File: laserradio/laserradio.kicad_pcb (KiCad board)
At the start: 2 copper layers, 84 parts, among them J1 USB4105-GF-A, J2 Conn_01x01_Female, J3 DEBUG, J4 RIGHT, SW1 SW_SPDT, SW2 SW_SPDT, U1 W25Q128JV, U2 RP2040, U3 MCP1702T-3302E_CB, U4 ADA4891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

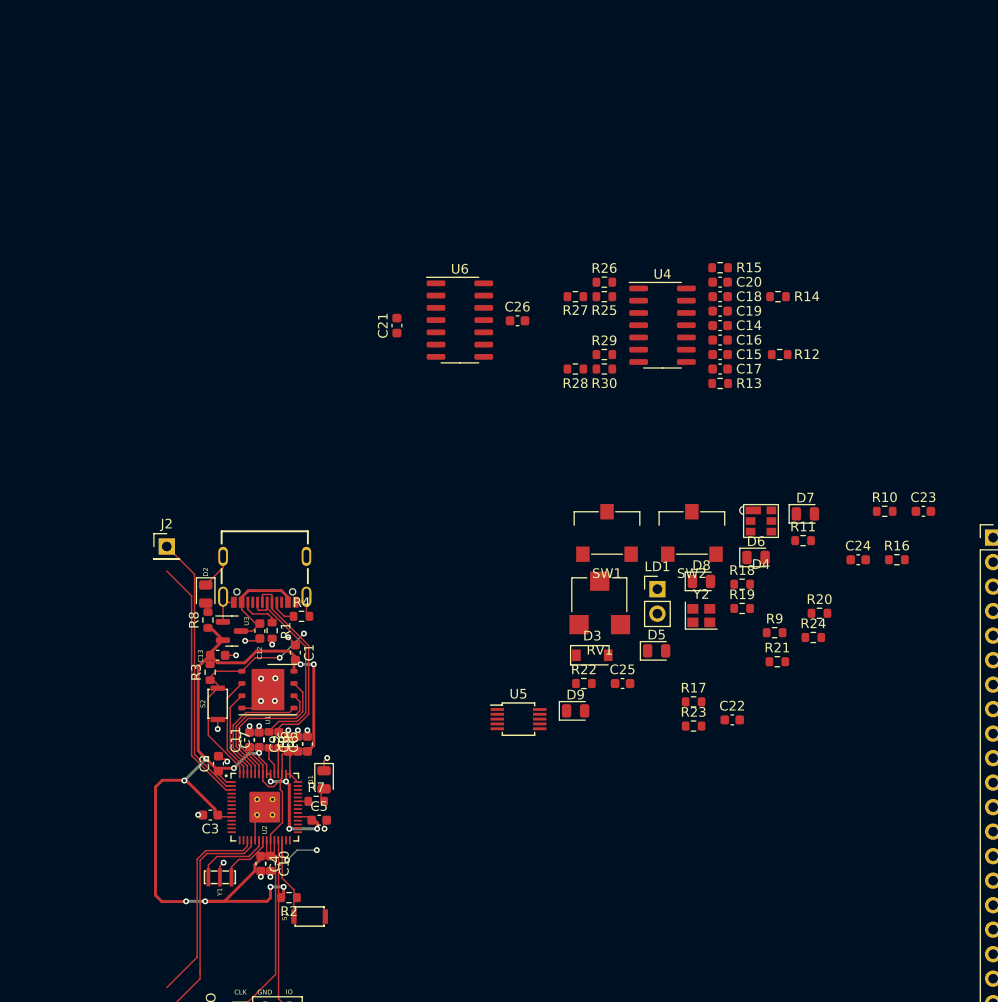
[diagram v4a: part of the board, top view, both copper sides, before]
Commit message: wip arranging op-amp filters
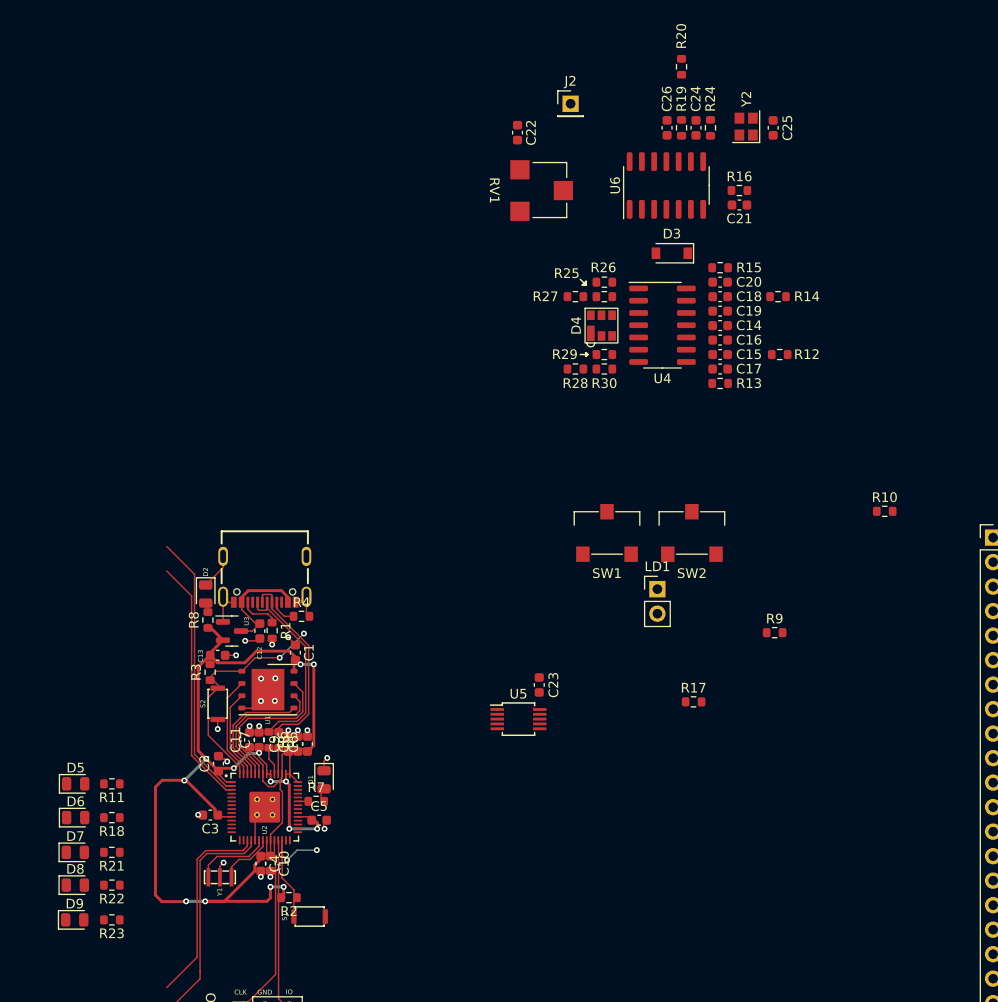
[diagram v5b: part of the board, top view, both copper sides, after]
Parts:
- moved D7 83.4 mm to (94.7, 104.6)
- moved R11 76.0 mm to (98.5, 97.5), turned to 180 degrees
- moved D6 75.5 mm to (94.7, 101.0)
- moved D8 72.1 mm to (94.7, 108.0)
- moved R21 71.8 mm to (98.5, 104.6), turned to 180 degrees
- moved R18 69.7 mm to (98.5, 101.0), turned to 180 degrees
- moved C22 64.8 mm to (140.5, 30.0), turned to -90 degrees
- moved R23 63.6 mm to (98.5, 111.6), turned to 180 degrees
- moved J2 62.1 mm to (146.0, 27.0)
- moved D5 61.8 mm to (94.7, 97.5)
- moved C25 59.7 mm to (167.0, 29.5), turned to 90 degrees
- moved R20 58.4 mm to (157.5, 23.2), turned to 90 degrees
- moved D9 56.3 mm to (94.6, 111.6)
- moved R24 53.9 mm to (160.5, 29.5), turned to -90 degrees
- moved R22 53.2 mm to (98.5, 108.0), turned to 180 degrees
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
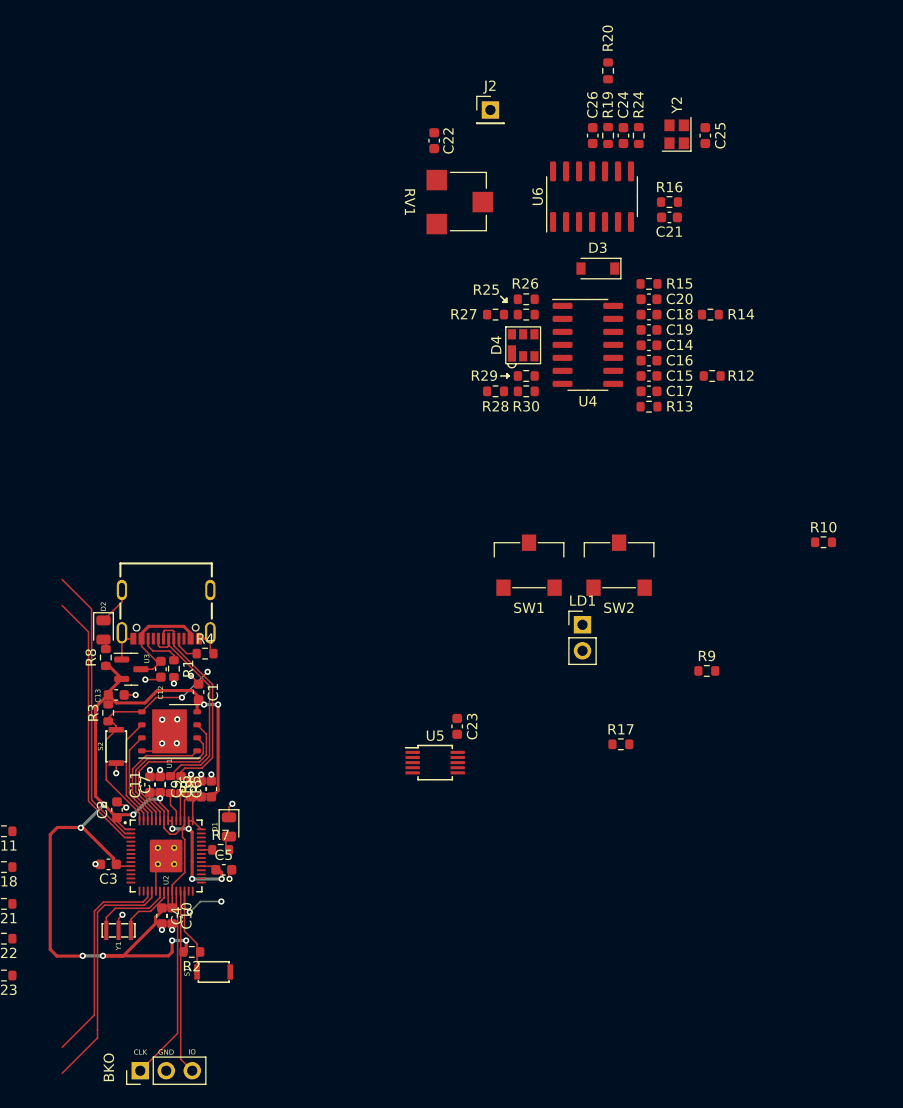
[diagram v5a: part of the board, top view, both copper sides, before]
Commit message: finish first pass of laying out components
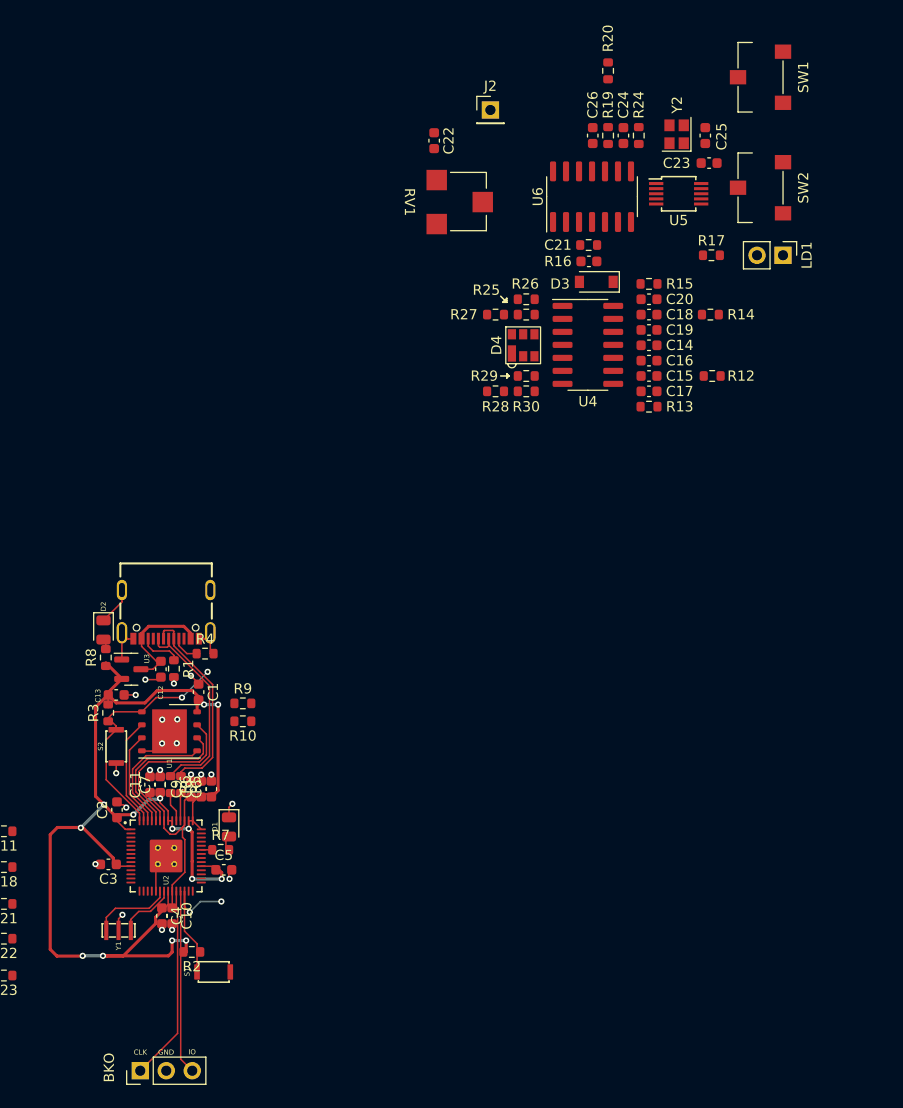
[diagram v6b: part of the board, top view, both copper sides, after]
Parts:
- moved U5 60.5 mm to (164.4, 35.2)
- moved C23 60.3 mm to (167.4, 32.2), turned to 0 degrees
- moved R10 59.4 mm to (121.8, 86.8), turned to 180 degrees
- moved SW1 52.8 mm to (172.4, 23.8), turned to 90 degrees
- moved R17 48.6 mm to (167.6, 41.2)
- moved R9 45.5 mm to (121.8, 85.0)
- moved LD1 41.1 mm to (174.6, 41.2), turned to -90 degrees
- moved SW2 39.4 mm to (172.4, 34.6), turned to 90 degrees
- moved C21 8.97 mm to (155.6, 41.8), turned to 0 degrees
- moved R16 8.95 mm to (155.6, 40.2), turned to 180 degrees
- moved D3 1.31 mm to (156.3, 43.8)
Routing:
- net +3V3: track 230.9 -> 203.0 mm
- net /Tx: track 25.8 -> 0.00 mm
- net /GPIO15: track 23.7 -> 0.00 mm
- net /GPIO14: track 21.0 -> 0.00 mm

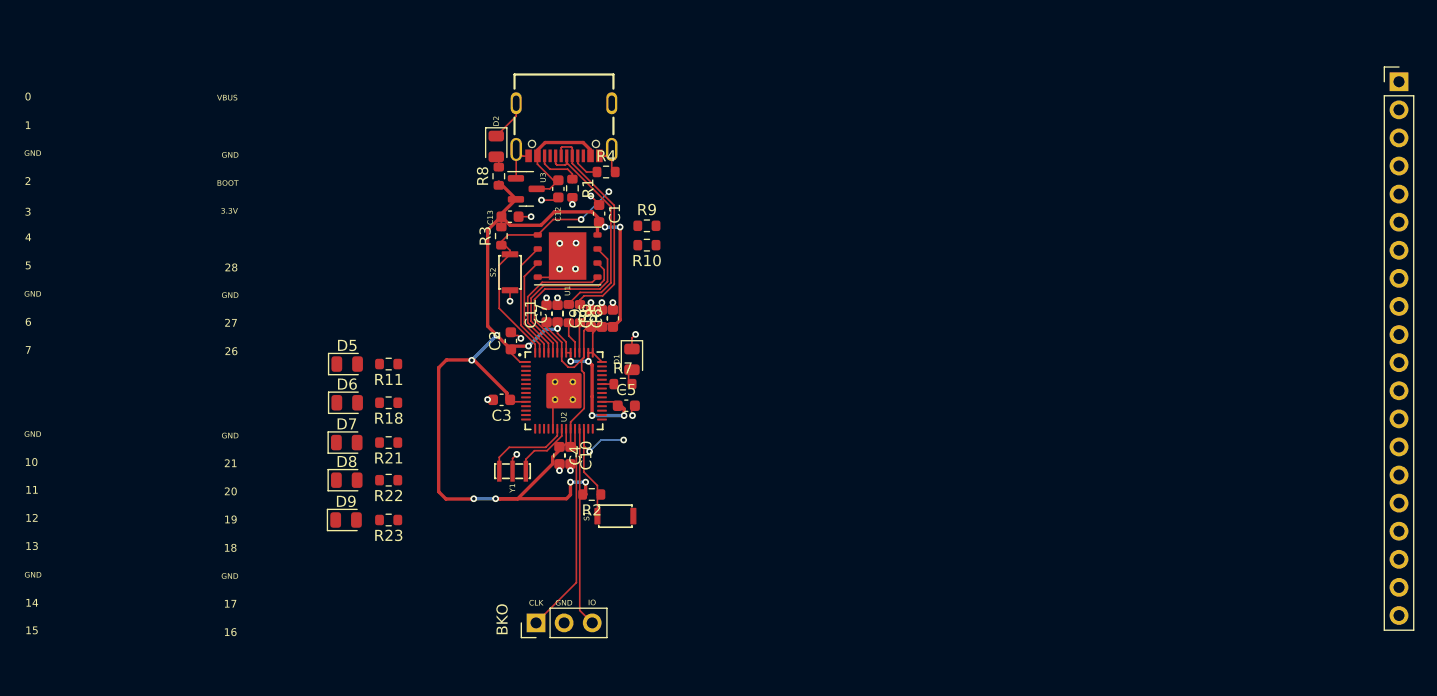
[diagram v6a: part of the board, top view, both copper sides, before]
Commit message: Refactored MP3 circuit
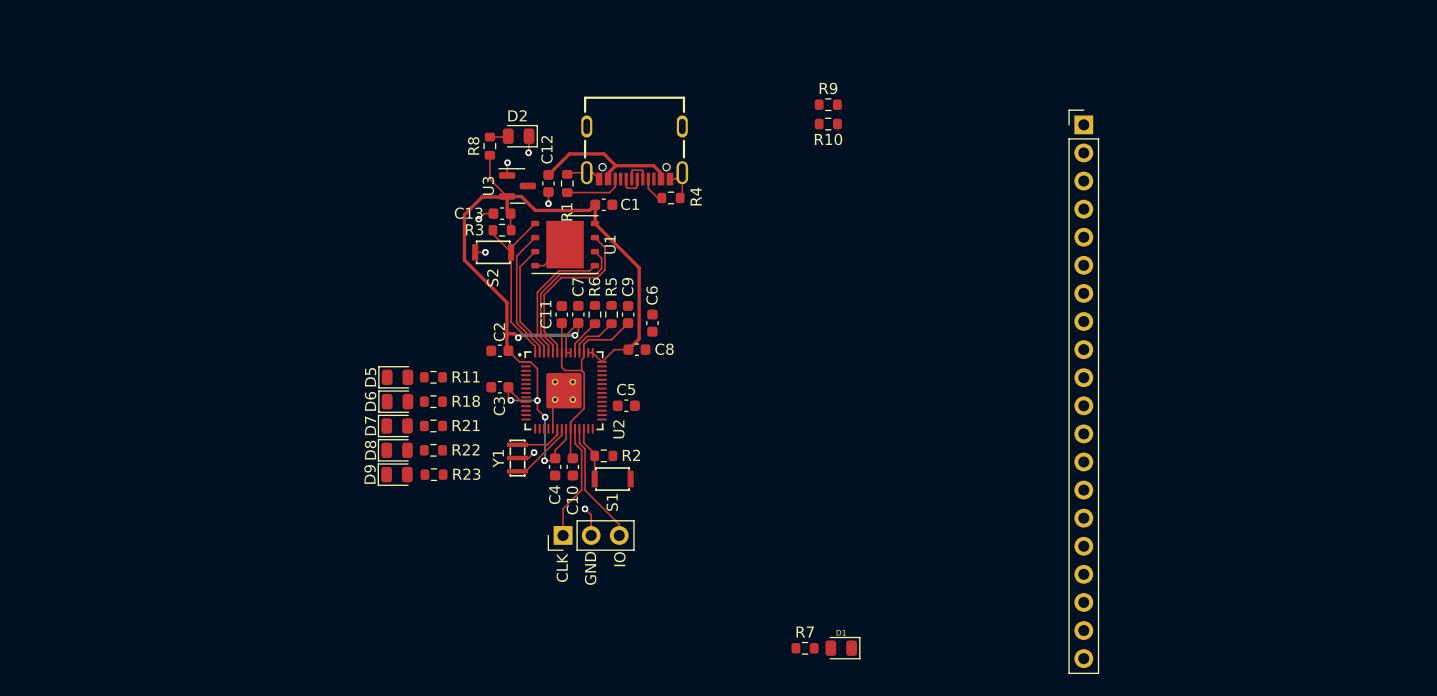
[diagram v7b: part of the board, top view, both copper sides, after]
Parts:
- moved D1 32.2 mm to (139.4, 123.2), turned to 180 degrees
- moved R7 29.0 mm to (136.1, 123.2)
- moved J4 28.8 mm to (161.3, 75.9)
- moved R10 19.7 mm to (138.2, 75.8)
- moved R9 19.7 mm to (138.2, 74.0)
- moved J3 8.27 mm to (114.2, 113.0)
- moved J1 6.72 mm to (120.7, 76.0)
- moved R4 6.32 mm to (124.0, 82.5)
- moved D9 6.16 mm to (99.2, 107.5)
- moved R23 5.80 mm to (102.5, 107.5)
- moved D8 5.29 mm to (99.2, 105.3)
- moved R22 4.87 mm to (102.5, 105.3)
- moved D7 4.79 mm to (99.2, 103.1)
- moved D5 4.71 mm to (99.2, 98.7)
- moved D6 4.55 mm to (99.2, 100.9)
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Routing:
- net +3V3: track 203.0 -> 87.5 mm, vias 16 -> 6
- net Net-(C10-Pad1): track 0.00 -> 21.8 mm
- net Net-(J1-PadA6): track 21.2 -> 3.13 mm
- net Net-(J1-PadA7): track 20.1 -> 2.52 mm
- net Net-(U1-Pad7): track 0.00 -> 15.5 mm
- net /SWDIO: track 0.00 -> 11.1 mm
- net /SWCLK: track 0.00 -> 10.6 mm
- net /RUN: track 14.2 -> 4.95 mm, vias 2 -> 0
- net GND: track 33.9 -> 24.8 mm, vias 19 -> 7
- net /BOOT: track 23.7 -> 16.2 mm, vias 2 -> 0
- net Net-(U2-Pad21): track 0.00 -> 5.93 mm
- net Net-(U2-Pad20): track 7.94 -> 4.52 mm
- net Net-(D1-Pad2): track 1.42 -> 0.00 mm
- net Net-(R5-Pad2): track 3.05 -> 4.45 mm
- net /GPIO25: track 1.39 -> 0.00 mm
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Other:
- board text removed: "0"
- board text removed: "1"
- board text removed: "10"
- board text removed: "11"
- board text removed: "12"
- board text removed: "13"
- board text removed: "14"
- board text removed: "15"
- board text removed: "16"
- board text removed: "17"
- board text removed: "18"
- board text removed: "19"
- board text removed: "2"
- board text removed: "20"
- board text removed: "21"
- board text removed: "26"
- board text removed: "27"
- board text removed: "28"
- board text removed: "3"
- board text removed: "3.3V"
- board text removed: "4"
- board text removed: "5"
- board text removed: "6"
- board text removed: "7"
- board text removed: "BKO"
- board text removed: "BOOT"
- board text removed: "VBUS"
